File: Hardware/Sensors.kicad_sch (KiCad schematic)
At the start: 41 parts, among them U10 BMI270, U11 LIS3MDLTR, U12 BMP388, U13 AT7456E, U14 SN65HVD230, U8 ICM-42688-P, U9 W25Q128JVSIQ, Y2 27Mhz 20pF

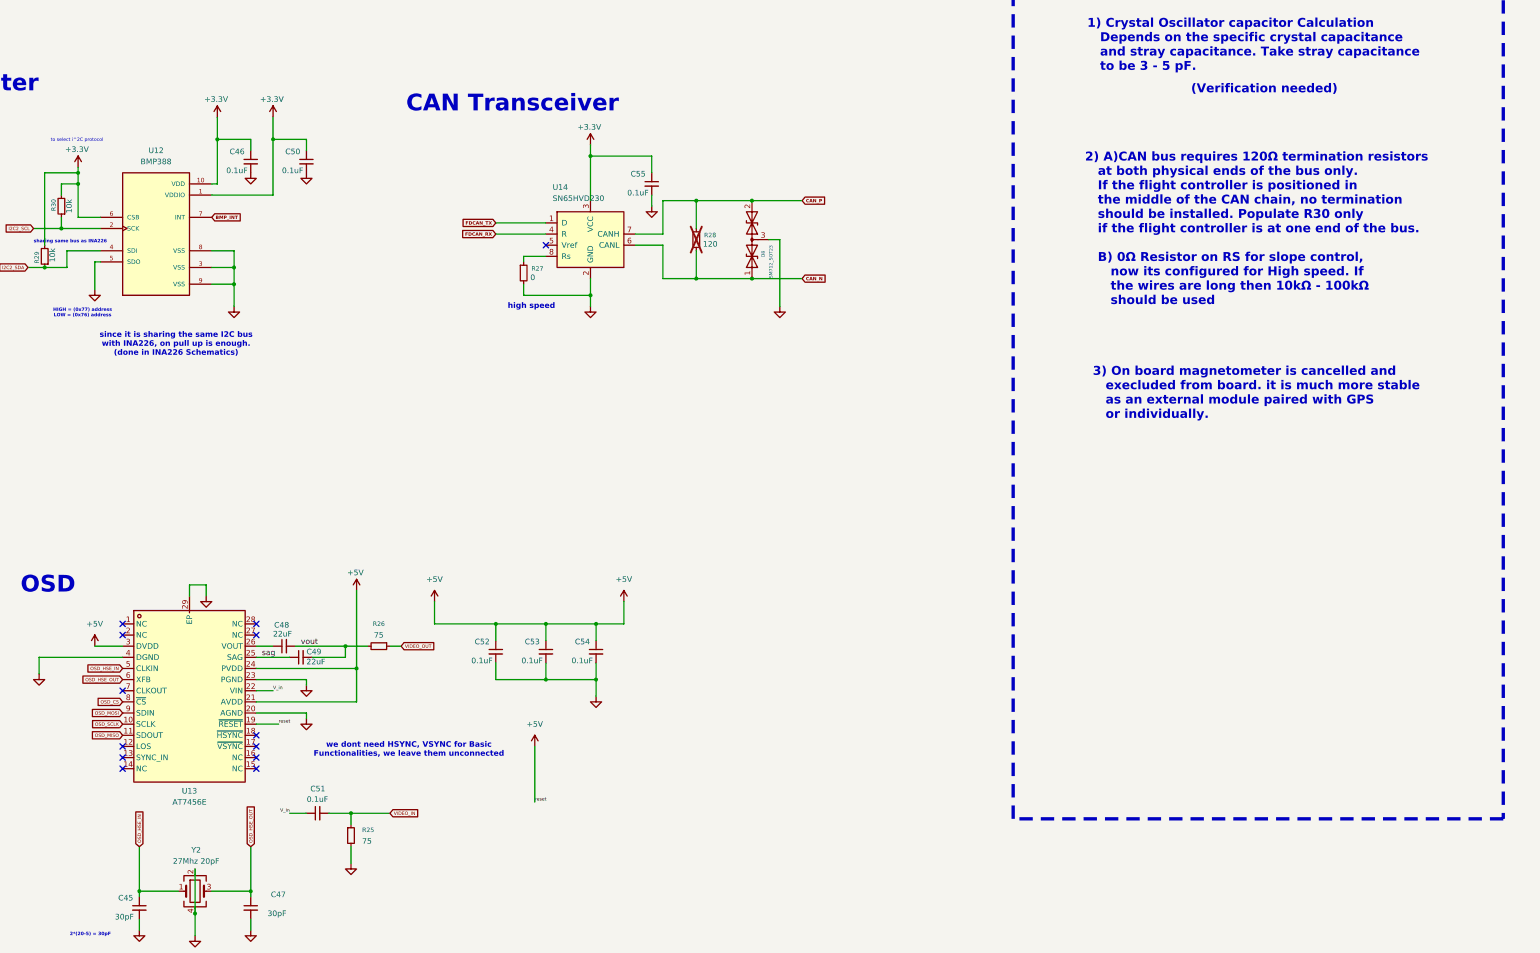
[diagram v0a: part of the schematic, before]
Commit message: added quatronion filter, CRSF protocol, and PID loops
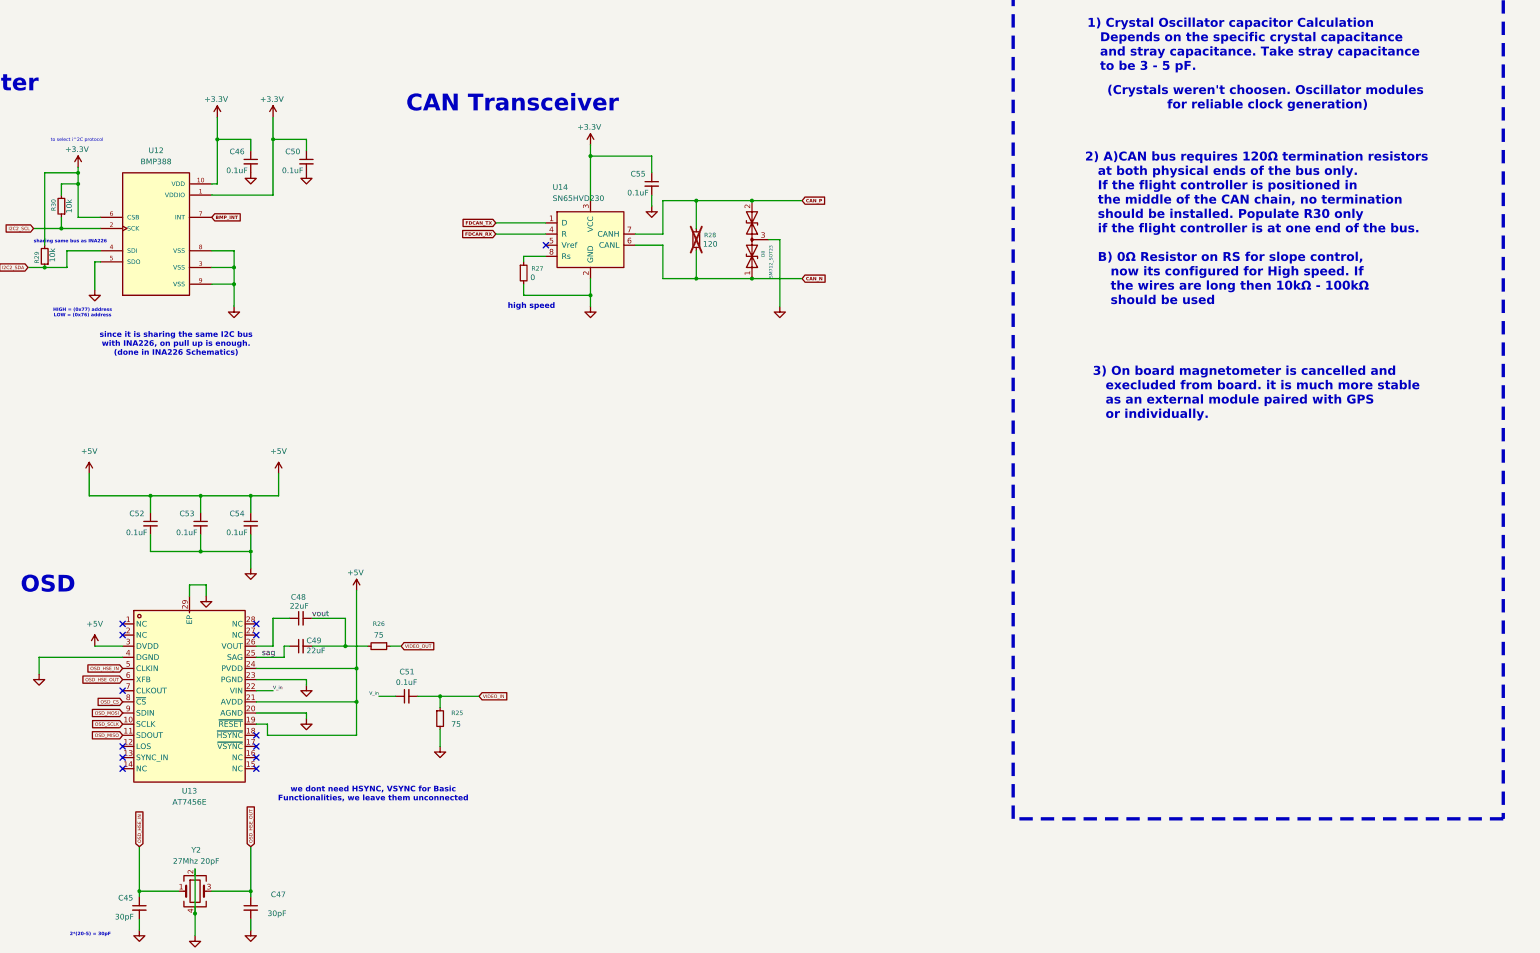
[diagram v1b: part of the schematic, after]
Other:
- note added: "(Crystals weren't choosen. Oscillator modules for reliable clock generation)"
- note removed: "(Verification needed)"
- moved on the sheet: C48, C49, C51, C52, C53, C54, R25

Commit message: added all drivers and usb CDC, motor mixing still not working
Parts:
- R29, R30: value 10k -> 7.5k
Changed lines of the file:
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@@
 			)
 		)
-		(property "Value" "10k"
+		(property "Value" "7.5k"
 			(at 282.448 81.28 90)
 			(show_name no)
@@
 			)
 		)
-		(property "Value" "10k"
+		(property "Value" "7.5k"
 			(at 278.638 92.456 90)
 			(show_name no)
